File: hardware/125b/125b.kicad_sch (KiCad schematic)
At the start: 58 parts, among them J1 Guitar in, J10 Barrel_Jack, J11 NRJ6HF, J2 fsw pin 7, J3 fsw pin 2, J4 fsw pin 7, J5 fsw pin 5, J6 fsw pin 6, J7 fsw pin 3, J8 fsw pin 4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

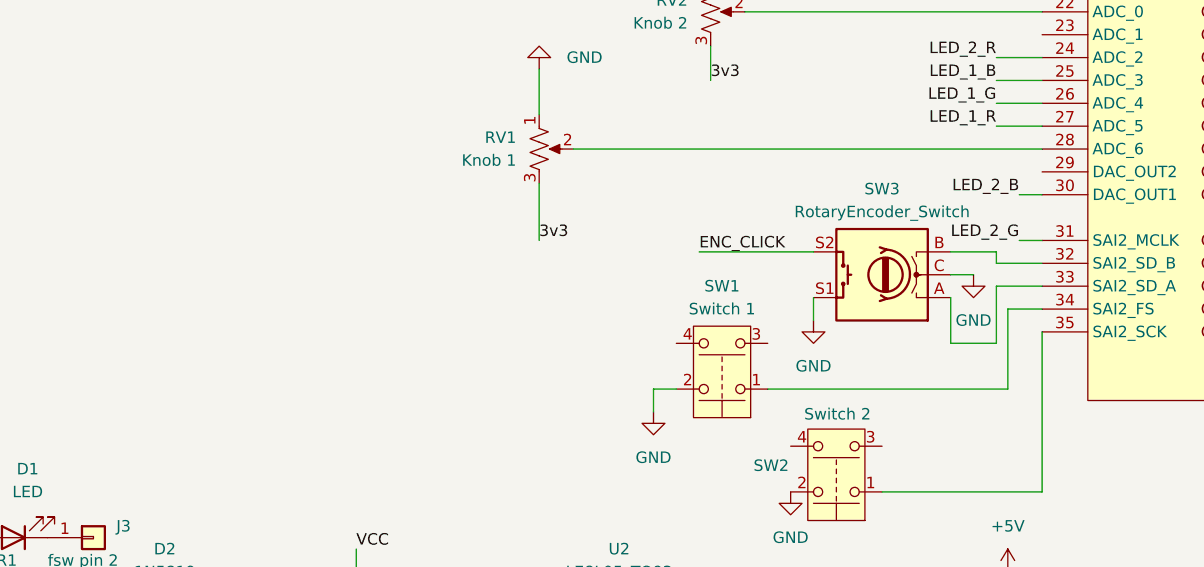
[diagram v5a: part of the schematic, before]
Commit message: Swap encoder pins
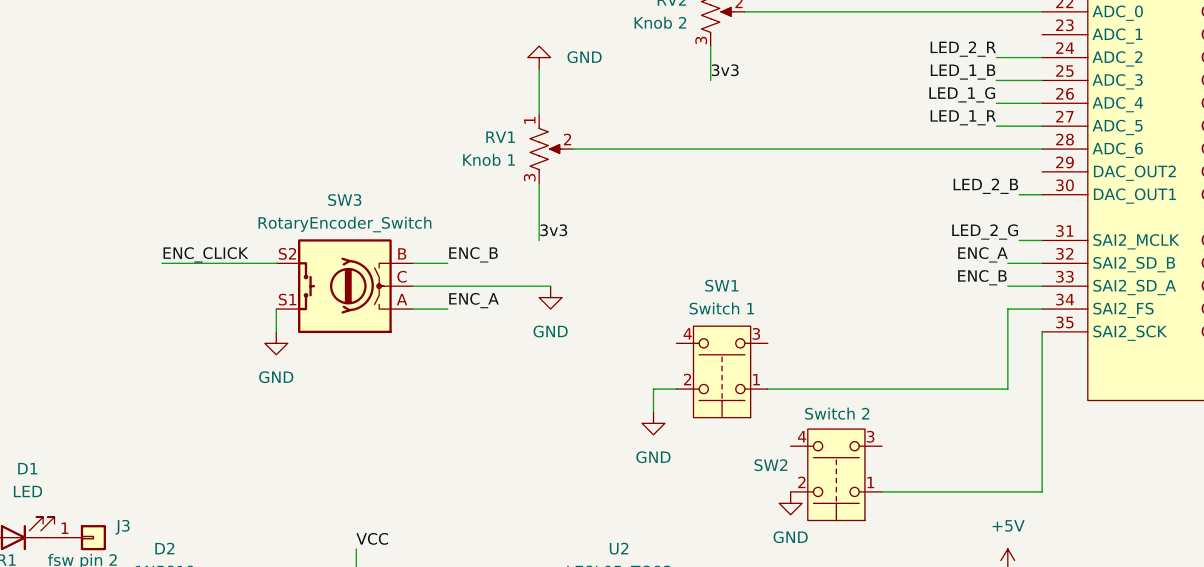
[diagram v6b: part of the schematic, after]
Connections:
- net ENC_A: now reaches SW3.A
- net ENC_A: now also A1.32 (SAI2_SD_B); no longer A1.33 (SAI2_SD_A)
- net ENC_B: now reaches SW3.B
- net ENC_B: now also A1.33 (SAI2_SD_A); no longer A1.32 (SAI2_SD_B)
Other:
- moved on the sheet: SW3
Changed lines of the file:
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@@
 	(wire
 		(pts
-			(xy 127 127) (xy 127 132.08)
-		)
-		(stroke
-			(width 0)
-			(type default)
-		)
-	)
-	(wire
-		(pts
 			(xy 73.66 179.07) (xy 73.66 190.5)
 		)
@@
 	(wire
 		(pts
-			(xy 137.16 123.19) (xy 132.08 123.19)
-		)
-		(stroke
-			(width 0)
-			(type default)
-		)
-	)
-	(wire
-		(pts
-			(xy 111.76 127) (xy 111.76 129.54)
+			(xy 52.07 128.27) (xy 52.07 130.81)
 		)
 		(stroke
@@
 	(wire
 		(pts
-			(xy 99.06 121.92) (xy 111.76 121.92)
+			(xy 39.37 123.19) (xy 52.07 123.19)
 		)
 		(stroke
@@
 	(wire
 		(pts
+			(xy 67.31 125.73) (xy 82.55 125.73)
+		)
+		(stroke
+			(width 0)
+			(type default)
+		)
+	)
+	(wire
+		(pts
 			(xy 26.67 52.07) (xy 26.67 53.34)
 		)
@@
 	(wire
 		(pts
-			(xy 133.35 161.29) (xy 133.35 171.45)
+			(xy 133.35 125.73) (xy 137.16 125.73)
 		)
 		(stroke
@@
 	(wire
 		(pts
-			(xy 252.73 95.25) (xy 262.89 95.25)
+			(xy 133.35 161.29) (xy 133.35 171.45)
 		)
 		(stroke
@@
 	(wire
 		(pts
-			(xy 101.6 53.34) (xy 105.41 53.34)
+			(xy 252.73 95.25) (xy 262.89 95.25)
 		)
 		(stroke
@@
 	(wire
 		(pts
-			(xy 260.35 67.31) (xy 261.62 67.31)
+			(xy 101.6 53.34) (xy 105.41 53.34)
 		)
 		(stroke
@@
 	(wire
 		(pts
-			(xy 243.84 67.31) (xy 243.84 74.93)
+			(xy 260.35 67.31) (xy 261.62 67.31)
 		)
 		(stroke
@@
 	(wire
 		(pts
-			(xy 85.09 110.49) (xy 137.16 110.49)
+			(xy 243.84 67.31) (xy 243.84 74.93)
 		)
 		(stroke
@@
 	(wire
 		(pts
-			(xy 218.44 60.96) (xy 218.44 64.77)
+			(xy 85.09 110.49) (xy 137.16 110.49)
 		)
 		(stroke
@@
 	(wire
 		(pts
-			(xy 132.08 107.95) (xy 137.16 107.95)
+			(xy 218.44 60.96) (xy 218.44 64.77)
 		)
 		(stroke
@@
 	(wire
 		(pts
-			(xy 132.08 125.73) (xy 137.16 125.73)
+			(xy 132.08 107.95) (xy 137.16 107.95)
 		)
 		(stroke
@@
 	(wire
 		(pts
-			(xy 132.08 125.73) (xy 132.08 132.08)
-		)
-		(stroke
-			(width 0)
-			(type default)
-		)
-	)
-	(wire
-		(pts
 			(xy 66.04 50.8) (xy 74.93 50.8)
 		)
@@
 	(wire
 		(pts
-			(xy 132.08 132.08) (xy 127 132.08)
-		)
-		(stroke
-			(width 0)
-			(type default)
-		)
-	)
-	(wire
-		(pts
 			(xy 90.17 168.91) (xy 90.17 189.23)
 		)
@@
 	(wire
 		(pts
-			(xy 132.08 123.19) (xy 132.08 121.92)
+			(xy 96.52 137.16) (xy 93.98 137.16)
 		)
 		(stroke
@@
 	(wire
 		(pts
-			(xy 127 124.46) (xy 129.54 124.46)
+			(xy 261.62 33.02) (xy 264.16 33.02)
 		)
 		(stroke
@@
 	(wire
 		(pts
-			(xy 96.52 137.16) (xy 93.98 137.16)
+			(xy 19.05 161.29) (xy 19.05 168.91)
 		)
 		(stroke
@@
 	(wire
 		(pts
-			(xy 261.62 33.02) (xy 264.16 33.02)
+			(xy 203.2 64.77) (xy 205.74 64.77)
 		)
 		(stroke
@@
 	(wire
 		(pts
-			(xy 19.05 161.29) (xy 19.05 168.91)
+			(xy 81.28 101.6) (xy 81.28 106.68)
 		)
 		(stroke
@@
 	(wire
 		(pts
-			(xy 203.2 64.77) (xy 205.74 64.77)
+			(xy 214.63 30.48) (xy 224.79 30.48)
 		)
 		(stroke
@@
 	(wire
 		(pts
-			(xy 81.28 101.6) (xy 81.28 106.68)
+			(xy 93.98 137.16) (xy 93.98 139.7)
 		)
 		(stroke
@@
 	(wire
 		(pts
-			(xy 127 121.92) (xy 132.08 121.92)
+			(xy 67.31 128.27) (xy 71.12 128.27)
 		)
 		(stroke
@@
 	(wire
 		(pts
-			(xy 214.63 30.48) (xy 224.79 30.48)
+			(xy 120.65 82.55) (xy 137.16 82.55)
 		)
 		(stroke
@@
 	(wire
 		(pts
-			(xy 93.98 137.16) (xy 93.98 139.7)
+			(xy 73.66 161.29) (xy 82.55 161.29)
 		)
 		(stroke
@@
 	(wire
 		(pts
-			(xy 120.65 82.55) (xy 137.16 82.55)
+			(xy 19.05 182.88) (xy 44.45 182.88)
 		)
 		(stroke
@@
 	(wire
 		(pts
-			(xy 73.66 161.29) (xy 82.55 161.29)
+			(xy 120.65 161.29) (xy 120.65 168.91)
 		)
 		(stroke
@@
 	(wire
 		(pts
-			(xy 19.05 182.88) (xy 44.45 182.88)
+			(xy 201.93 64.77) (xy 203.2 64.77)
 		)
 		(stroke
@@
 	(wire
 		(pts
-			(xy 120.65 161.29) (xy 120.65 168.91)
+			(xy 137.16 130.81) (xy 137.16 148.59)
 		)
 		(stroke
@@
 	(wire
 		(pts
-			(xy 201.93 64.77) (xy 203.2 64.77)
+			(xy 224.79 35.56) (xy 224.79 41.91)
 		)
 		(stroke
@@
 	(wire
 		(pts
-			(xy 137.16 130.81) (xy 137.16 148.59)
+			(xy 67.31 123.19) (xy 71.12 123.19)
 		)
 		(stroke
@@
 	(wire
 		(pts
-			(xy 224.79 35.56) (xy 224.79 41.91)
+			(xy 133.35 123.19) (xy 137.16 123.19)
 		)
 		(stroke
@@
 	)
 	(label "ENC_CLICK"
-		(at 99.06 121.92 0)
+		(at 39.37 123.19 0)
 		(effects
 			(font
@@
 		)
 	)
+	(label "ENC_B"
+		(at 133.35 125.73 180)
+		(effects
+			(font
+				(size 1.27 1.27)
+			)
+			(justify right bottom)
+		)
+	)
+	(label "ENC_A"
+		(at 71.12 128.27 0)
+		(effects
+			(font
+				(size 1.27 1.27)
+			)
+			(justify left bottom)
+		)
+	)
 	(label "LED_1_G"
 		(at 132.08 105.41 180)
@@
 		)
 	)
+	(label "ENC_B"
+		(at 71.12 123.19 0)
+		(effects
+			(font
+				(size 1.27 1.27)
+			)
+			(justify left bottom)
+		)
+	)
 	(label "Left out"
 		(at 120.65 87.63 180)
@@
 		)
 	)
+	(label "ENC_A"
+		(at 133.35 123.19 180)
+		(effects
+			(font
+				(size 1.27 1.27)
+			)
+			(justify right bottom)
+		)
+	)
 	(label "3v3"
 		(at 100.33 102.87 0)
@@
 	(symbol
 		(lib_id "Device:RotaryEncoder_Switch")
-		(at 119.38 124.46 180)
+		(at 59.69 125.73 180)
 		(unit 1)
 		(exclude_from_sim no)
@@
 		(fields_autoplaced yes)
 		(property "Reference" "SW3"
-			(at 119.38 114.935 0)
+			(at 59.69 116.205 0)
 			(effects
 				(font
@@
 		)
 		(property "Value" "RotaryEncoder_Switch"
-			(at 119.38 117.475 0)
+			(at 59.69 118.745 0)
 			(effects
 				(font
@@
 		)
 		(property "Footprint" "Rotary_Encoder:RotaryEncoder_Alps_EC12E-Switch_Vertical_H20mm"
-			(at 123.19 128.524 0)
+			(at 63.5 129.794 0)
 			(effects
 				(font
@@
 		)
 		(property "Datasheet" "~"
-			(at 119.38 131.064 0)
+			(at 59.69 132.334 0)
 			(effects
 				(font
@@
 		)
 		(property "Description" ""
-			(at 119.38 124.46 0)
+			(at 59.69 125.73 0)
 			(effects
 				(font
@@
 		(lib_name "GND_10")
 		(lib_id "power:GND")
-		(at 129.54 124.46 0)
+		(at 82.55 125.73 0)
 		(unit 1)
 		(exclude_from_sim no)
@@
 		(fields_autoplaced yes)
 		(property "Reference" "#PWR016"
-			(at 129.54 130.81 0)
+			(at 82.55 132.08 0)
 			(effects
 				(font
@@
 		)
 		(property "Value" "GND"
-			(at 129.54 129.54 0)
+			(at 82.55 130.81 0)
 			(effects
 				(font
@@
 		)
 		(property "Footprint" ""
-			(at 129.54 124.46 0)
+			(at 82.55 125.73 0)
 			(effects
 				(font
@@
 		)
 		(property "Datasheet" ""
-			(at 129.54 124.46 0)
+			(at 82.55 125.73 0)
 			(effects
 				(font
@@
 		)
 		(property "Description" "Power symbol creates a global label with name \"GND\" , ground"
-			(at 129.54 124.46 0)
+			(at 82.55 125.73 0)
 			(effects
 				(font
@@
 		(lib_name "GND_13")
 		(lib_id "power:GND")
-		(at 111.76 129.54 0)
+		(at 52.07 130.81 0)
 		(unit 1)
 		(exclude_from_sim no)
@@
 		(fields_autoplaced yes)
 		(property "Reference" "#PWR014"
-			(at 111.76 135.89 0)
+			(at 52.07 137.16 0)
 			(effects
 				(font
@@
 		)
 		(property "Value" "GND"
-			(at 111.76 134.62 0)
+			(at 52.07 135.89 0)
 			(effects
 				(font
@@
 		)
 		(property "Footprint" ""
-			(at 111.76 129.54 0)
+			(at 52.07 130.81 0)
 			(effects
 				(font
@@
 		)
 		(property "Datasheet" ""
-			(at 111.76 129.54 0)
+			(at 52.07 130.81 0)
 			(effects
 				(font
@@
 		)
 		(property "Description" "Power symbol creates a global label with name \"GND\" , ground"
-			(at 111.76 129.54 0)
+			(at 52.07 130.81 0)
 			(effects
 				(font

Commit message: Components replaced on board after rejig
Back with the audio and power sockets on board
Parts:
- SW4: footprint Button_Switch_SMD:SW_DIP_SPSTx02_Slide_9.78x7.26mm_W8.61mm_P2.54mm -> Button_Switch_THT:SW_DIP_SPSTx02_Slide_9.78x7.26mm_W7.62mm_P2.54mm
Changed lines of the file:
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@@
 			)
 		)
-		(property "Footprint" "Button_Switch_SMD:SW_DIP_SPSTx02_Slide_9.78x7.26mm_W8.61mm_P2.54mm"
+		(property "Footprint" "Button_Switch_THT:SW_DIP_SPSTx02_Slide_9.78x7.26mm_W7.62mm_P2.54mm"
 			(at 34.29 53.34 0)
 			(effects

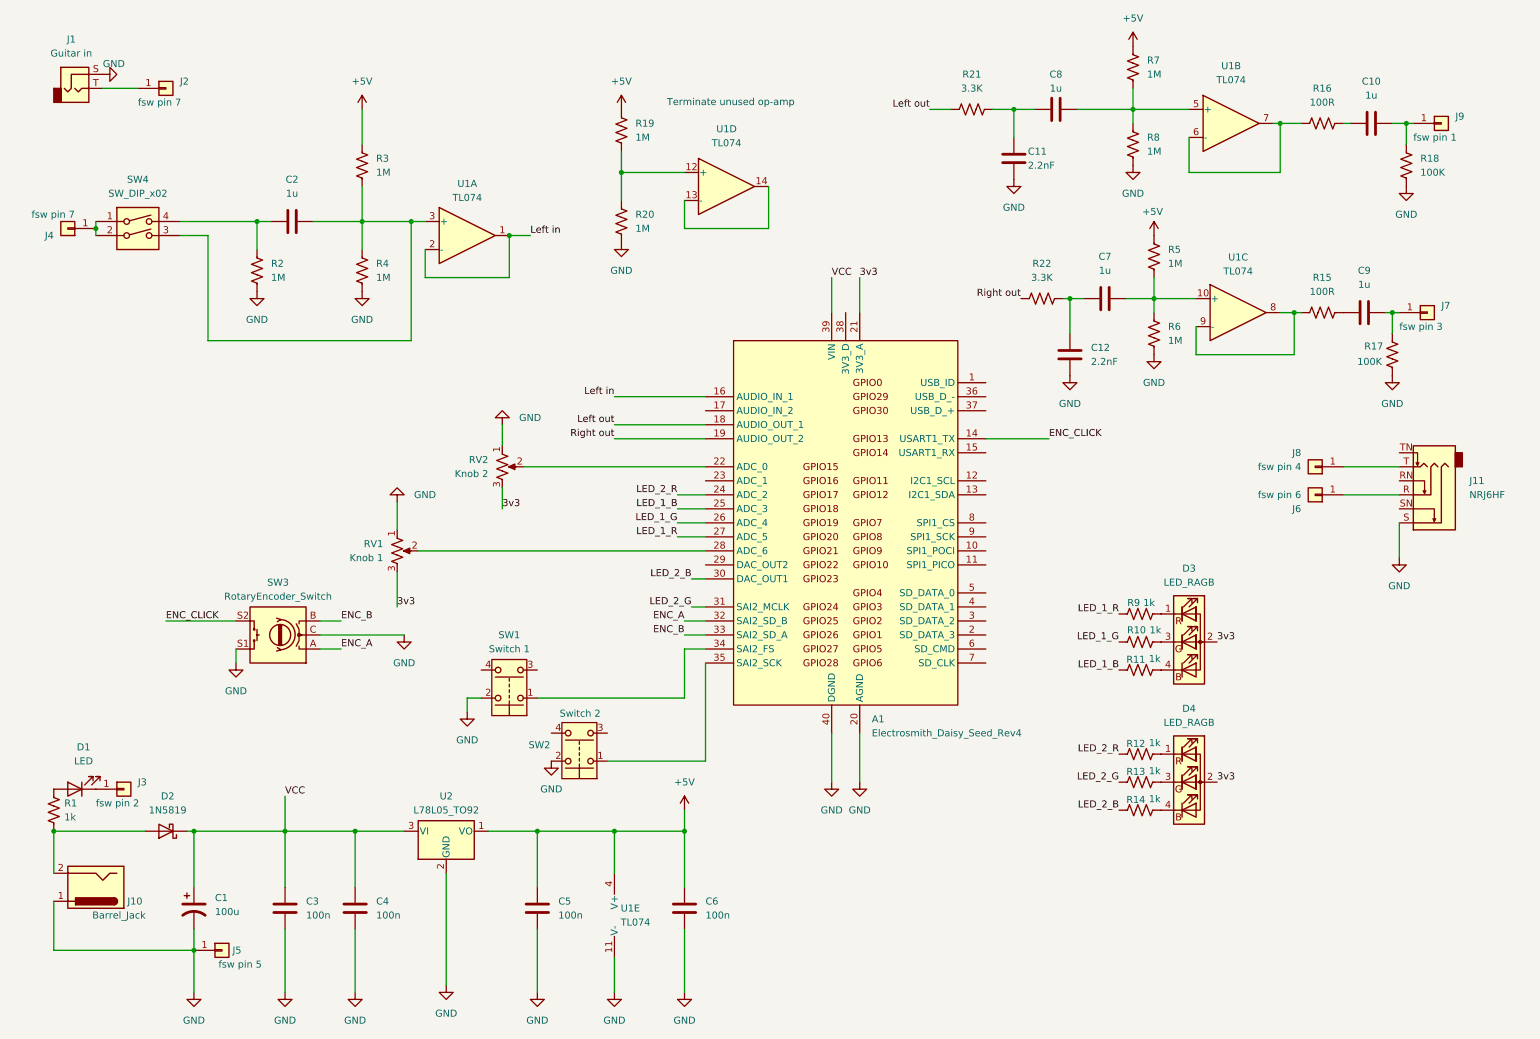
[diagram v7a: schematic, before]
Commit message: add a 3DPDT footswitch to kicad and then schematic
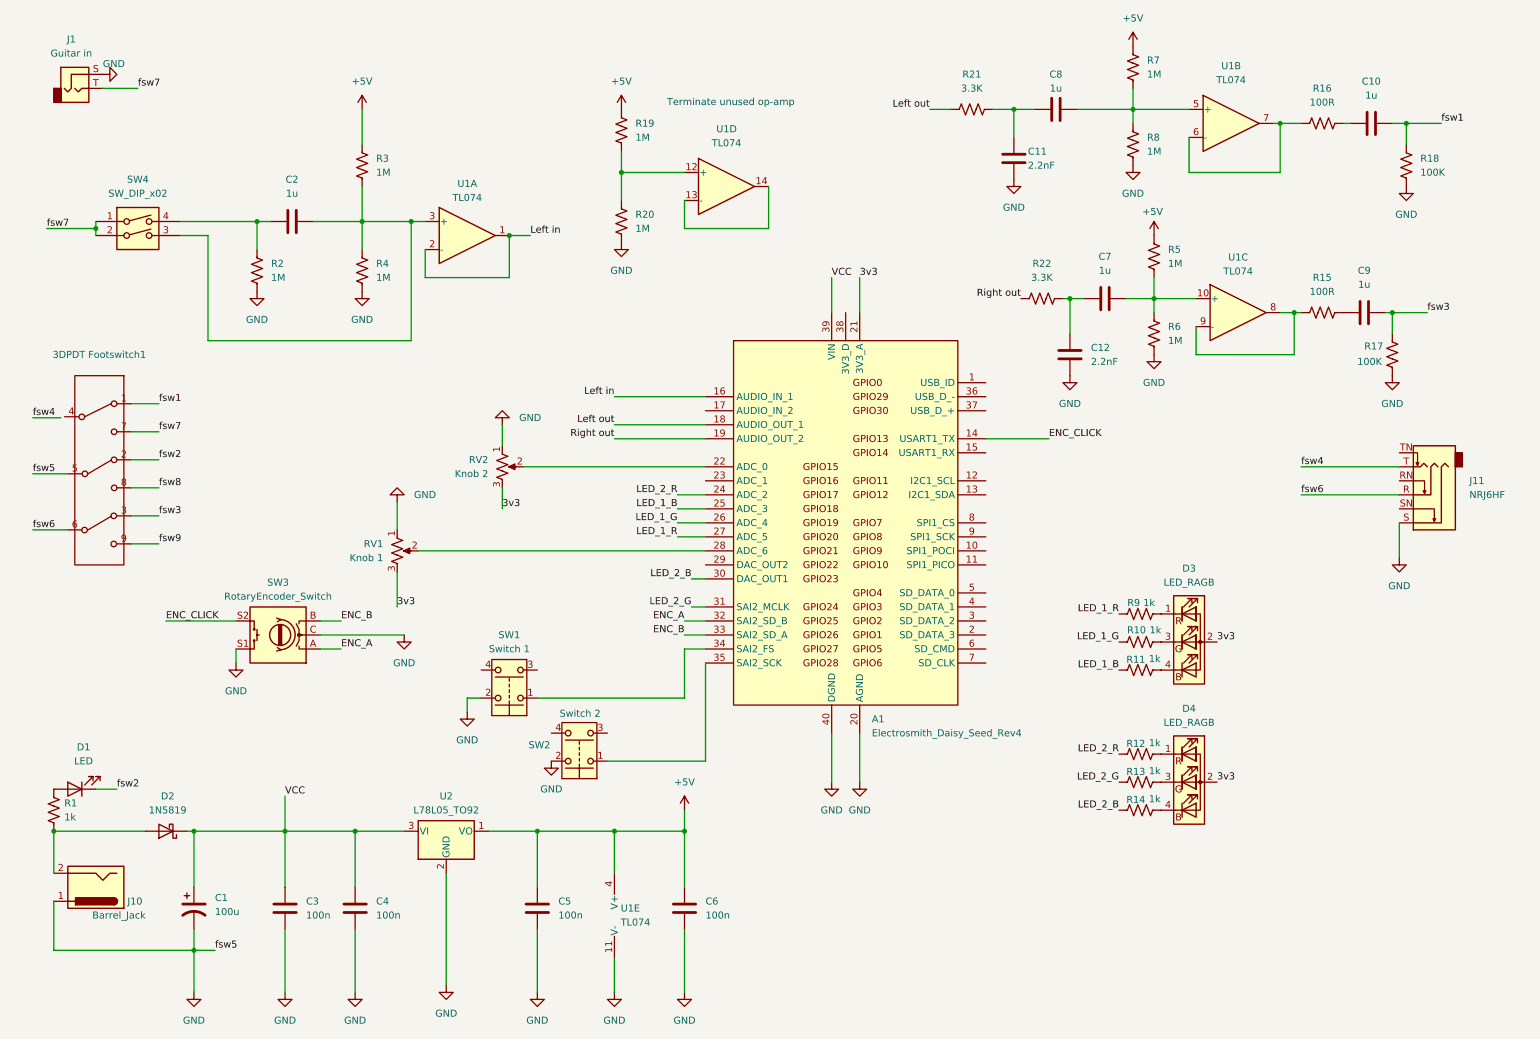
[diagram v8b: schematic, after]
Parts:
- removed J2, J4: fsw pin 7, Connector_Wire:SolderWire-0.25sqmm_1x01_D0.65mm_OD2mm, symbol Connector_Generic:Conn_01x01
- removed J3: fsw pin 2, Connector_Wire:SolderWire-0.25sqmm_1x01_D0.65mm_OD2mm, symbol Connector_Generic:Conn_01x01
- removed J5: fsw pin 5, Connector_Wire:SolderWire-0.25sqmm_1x01_D0.65mm_OD2mm, symbol Connector_Generic:Conn_01x01
- removed J6: fsw pin 6, Connector_Wire:SolderWire-0.25sqmm_1x01_D0.65mm_OD2mm, symbol Connector_Generic:Conn_01x01
- removed J7: fsw pin 3, Connector_Wire:SolderWire-0.25sqmm_1x01_D0.65mm_OD2mm, symbol Connector_Generic:Conn_01x01
- removed J8: fsw pin 4, Connector_Wire:SolderWire-0.25sqmm_1x01_D0.65mm_OD2mm, symbol Connector_Generic:Conn_01x01
- removed J9: fsw pin 1, Connector_Wire:SolderWire-0.25sqmm_1x01_D0.65mm_OD2mm, symbol Connector_Generic:Conn_01x01
- added 3DPDT Footswitch1: ~, symbol Switch:SW_3DPDT
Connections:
- net GND: now also 3DPDT Footswitch1.5 (E)
- net fsw4: now reaches J11.T
- net fsw1: now reaches C10.2, R18.1
- net fsw1: now also 3DPDT Footswitch1.1 (A)
- net fsw3: now reaches C9.2, R17.1
- net fsw3: now also 3DPDT Footswitch1.3 (C)
- net fsw6: now reaches J11.R
- net fsw6: now also 3DPDT Footswitch1.6 (F)
- net fsw7: now reaches J1.T
- net fsw7: now also SW4.1, SW4.2, 3DPDT Footswitch1.7 (G)
- net fsw2: now reaches D1.1 (K)
- net fsw2: now also 3DPDT Footswitch1.2 (B)
- new net fsw8: 3DPDT Footswitch1.8 (G)
- new net fsw9: 3DPDT Footswitch1.9 (G)
